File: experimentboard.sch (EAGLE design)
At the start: 168 parts, among them IC1 TL072P, IC2 LM317, IC3 LM337, IC4 TL072P, IC5 TL072P, IC6 TL072P, U1 PCM1690, U2 DIR9001, U3 CAT24C256

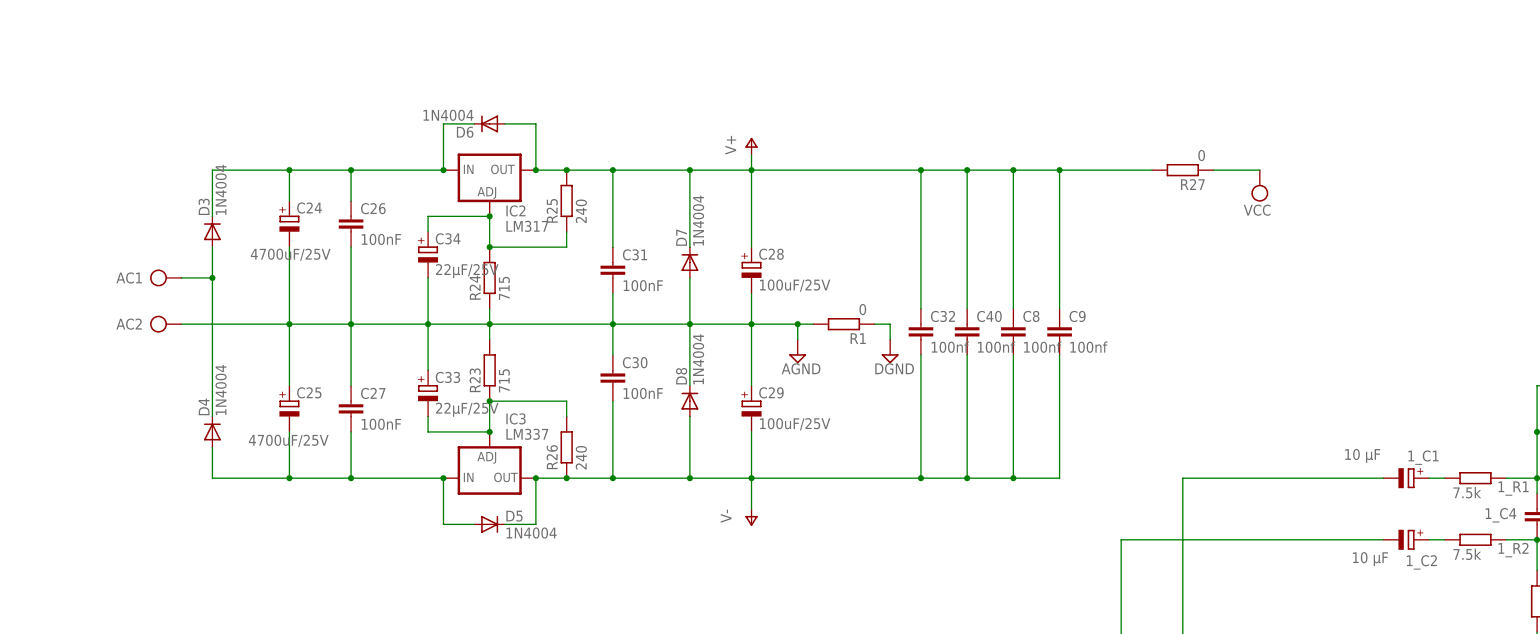
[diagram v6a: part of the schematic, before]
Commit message: Mostly the analog section, routing and squeezing
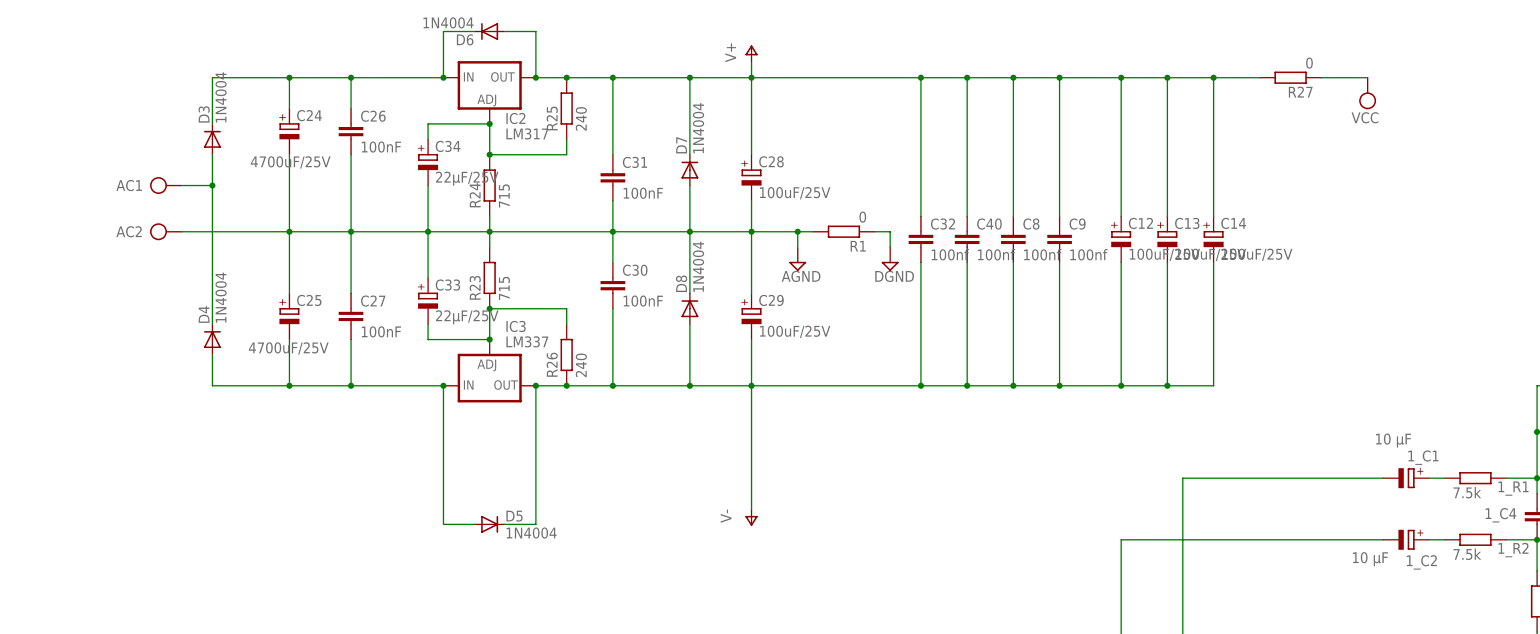
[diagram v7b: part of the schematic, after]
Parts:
- added C12, C13, C14: 100uF/25V, rcl:CPOL-EUE2.5-6
- 2_R7, 4_R7, 6_R7, 8_R7: device rcl:R-EU_0207/10 -> rcl:R-EU_0207/7
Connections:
- net V+: now also C12.+, C13.+, C14.+
- net V-: now also C12.-, C13.-, C14.-
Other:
- moved on the sheet: AC1, AC2, C24, C25, C26, C27, C28, C29, C30, C31, C32, C33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

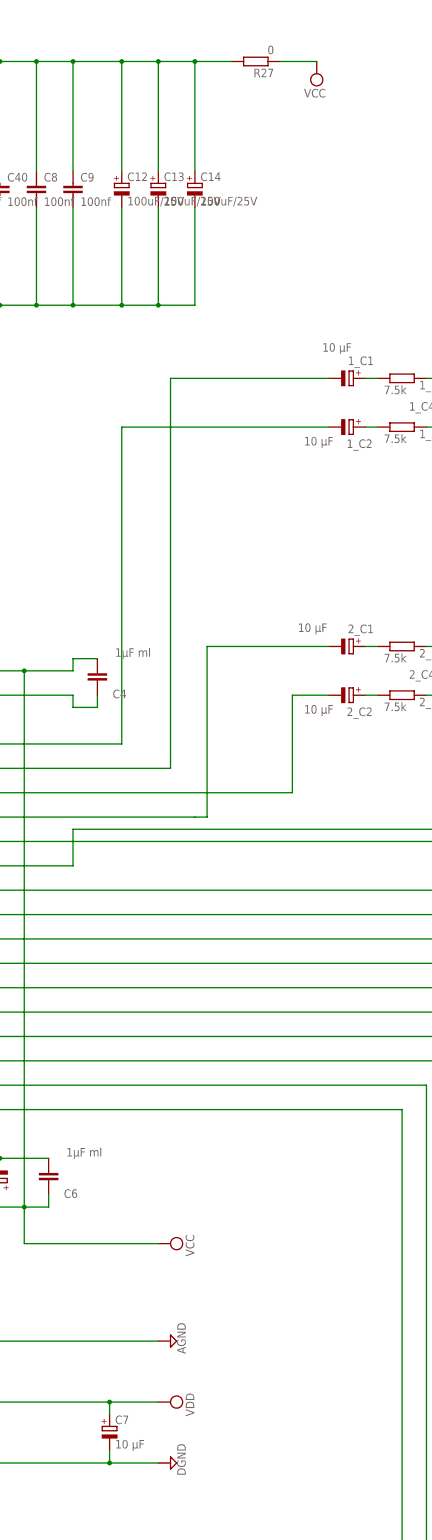
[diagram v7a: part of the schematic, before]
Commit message: Rotated PSU section, and more work since
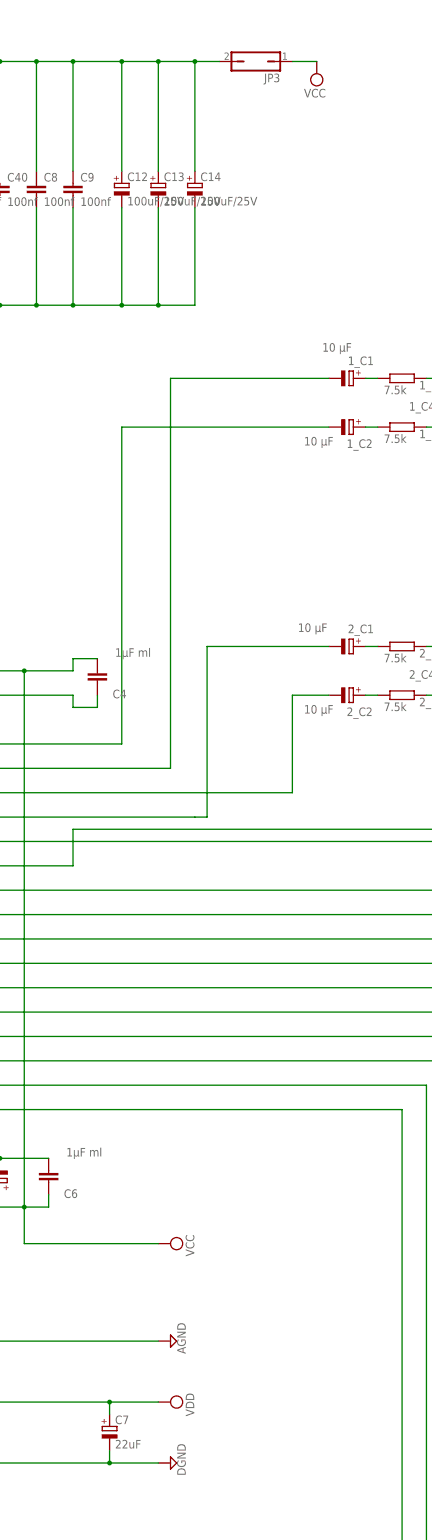
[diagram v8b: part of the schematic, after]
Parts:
- removed R27: 0, rcl:R-EU_0207/10
- added JP3: (no value), jumper:JP1Q
- C3: device rcl:CPOL-EUE1.8-4 -> rcl:CPOL-EUE2-5
- C7: value 10 µF -> 22uF; device rcl:CPOL-EUE1.8-4 -> rcl:CPOL-EUE2-5
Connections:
- net N$12 renamed VCOM
- net V+: now also JP3.2; no longer R27.2
- net VCC: now also JP3.1; no longer R27.1
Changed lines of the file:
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@@
 <part name="R4" library="rcl" deviceset="R-EU_" device="0207/7" value="22"/>
 <part name="SUPPLY3" library="supply2" deviceset="AGND" device=""/>
-<part name="C3" library="rcl" deviceset="CPOL-EU" device="E1.8-4" value="10 µF"/>
+<part name="C3" library="rcl" deviceset="CPOL-EU" device="E2-5" value="10 µF"/>
 <part name="SUPPLY5" library="supply2" deviceset="VDD" device=""/>
 <part name="SUPPLY6" library="supply2" deviceset="DGND" device=""/>
@@
 <part name="R7" library="rcl" deviceset="R-EU_" device="0207/7" value="10k"/>
 <part name="SUPPLY7" library="supply2" deviceset="VCC" device=""/>
-<part name="C7" library="rcl" deviceset="CPOL-EU" device="E1.8-4" value="10 µF"/>
+<part name="C7" library="rcl" deviceset="CPOL-EU" device="E2-5" value="22uF"/>
 <part name="IC1" library="0000halfgaar" deviceset="TL072" device="P"/>
 <part name="1_R1" library="rcl" deviceset="R-EU_" device="0207/7" value="7.5k"/>
@@
 <part name="R1" library="rcl" deviceset="R-EU_" device="0207/10" value="0"/>
 <part name="SUPPLY13" library="supply2" deviceset="DGND" device=""/>
-<part name="R27" library="rcl" deviceset="R-EU_" device="0207/10" value="0"/>
 <part name="SUPPLY27" library="supply2" deviceset="VCC" device=""/>
 <part name="SUPPLY28" library="supply2" deviceset="VCC" device=""/>
@@
 <part name="C13" library="rcl" deviceset="CPOL-EU" device="E2.5-6" value="100uF/25V"/>
 <part name="C14" library="rcl" deviceset="CPOL-EU" device="E2.5-6" value="100uF/25V"/>
+<part name="JP3" library="jumper" deviceset="JP1Q" device=""/>
 </parts>
 <sheets>
@@
 <instance part="R1" gate="G$1" x="124.46" y="215.9" rot="R180"/>
 <instance part="SUPPLY13" gate="G$1" x="132.08" y="210.82"/>
-<instance part="R27" gate="G$1" x="198.12" y="241.3" rot="R180"/>
 <instance part="SUPPLY27" gate="G$1" x="210.82" y="238.76" rot="R180"/>
 <instance part="SUPPLY28" gate="G$1" x="-101.6" y="93.98"/>
@@
 <instance part="C13" gate="G$1" x="177.8" y="215.9"/>
 <instance part="C14" gate="G$1" x="185.42" y="215.9"/>
+<instance part="JP3" gate="A" x="198.12" y="241.3" rot="R90"/>
 </instances>
 <busses>
@@
 </segment>
 </net>
-<net name="N$12" class="0">
+<net name="VCOM" class="0">
 <segment>
 <pinref part="U1" gate="U$1" pin="VCOM"/>
@@
 </segment>
 <segment>
-<pinref part="R27" gate="G$1" pin="1"/>
-<pinref part="SUPPLY27" gate="G$1" pin="VCC"/>
-<wire x1="203.2" y1="241.3" x2="210.82" y2="241.3" width="0.1524" layer="91"/>
-</segment>
-<segment>
 <pinref part="U$2" gate="G$1" pin="VDD_5V"/>
 <pinref part="SUPPLY28" gate="G$1" pin="VCC"/>
 <wire x1="-78.74" y1="83.82" x2="-101.6" y2="83.82" width="0.1524" layer="91"/>
 <wire x1="-101.6" y1="83.82" x2="-101.6" y2="91.44" width="0.1524" layer="91"/>
+</segment>
+<segment>
+<pinref part="JP3" gate="A" pin="1"/>
+<pinref part="SUPPLY27" gate="G$1" pin="VCC"/>
+<wire x1="205.74" y1="241.3" x2="210.82" y2="241.3" width="0.1524" layer="91"/>
 </segment>
 </net>
@@
 <pinref part="P+1" gate="1" pin="V+"/>
 <pinref part="C32" gate="G$1" pin="1"/>
-<pinref part="R27" gate="G$1" pin="2"/>
 <wire x1="137.16" y1="241.3" x2="144.78" y2="241.3" width="0.1524" layer="91"/>
 <junction x="137.16" y="241.3"/>
@@
 <wire x1="170.18" y1="241.3" x2="177.8" y2="241.3" width="0.1524" layer="91"/>
 <wire x1="177.8" y1="241.3" x2="185.42" y2="241.3" width="0.1524" layer="91"/>
-<wire x1="185.42" y1="241.3" x2="193.04" y2="241.3" width="0.1524" layer="91"/>
 <wire x1="144.78" y1="218.44" x2="144.78" y2="241.3" width="0.1524" layer="91"/>
 <junction x="144.78" y="241.3"/>
@@
 <pinref part="C14" gate="G$1" pin="+"/>
 <wire x1="185.42" y1="218.44" x2="185.42" y2="241.3" width="0.1524" layer="91"/>
+<pinref part="JP3" gate="A" pin="2"/>
+<wire x1="185.42" y1="241.3" x2="190.5" y2="241.3" width="0.1524" layer="91"/>
 <junction x="185.42" y="241.3"/>
 </segment>
@@
 </sheet>
 </sheets>
-<errors>
-</errors>
 </schematic>
 </drawing>
